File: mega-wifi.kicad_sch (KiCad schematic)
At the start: 25 parts, among them P2 MD-CART-FINGERS, U4 AZ1117CH-3.3, U5 74LVC1G08GW, U6 74LVC162245, U7 74LVC245, U8 74LVC162245

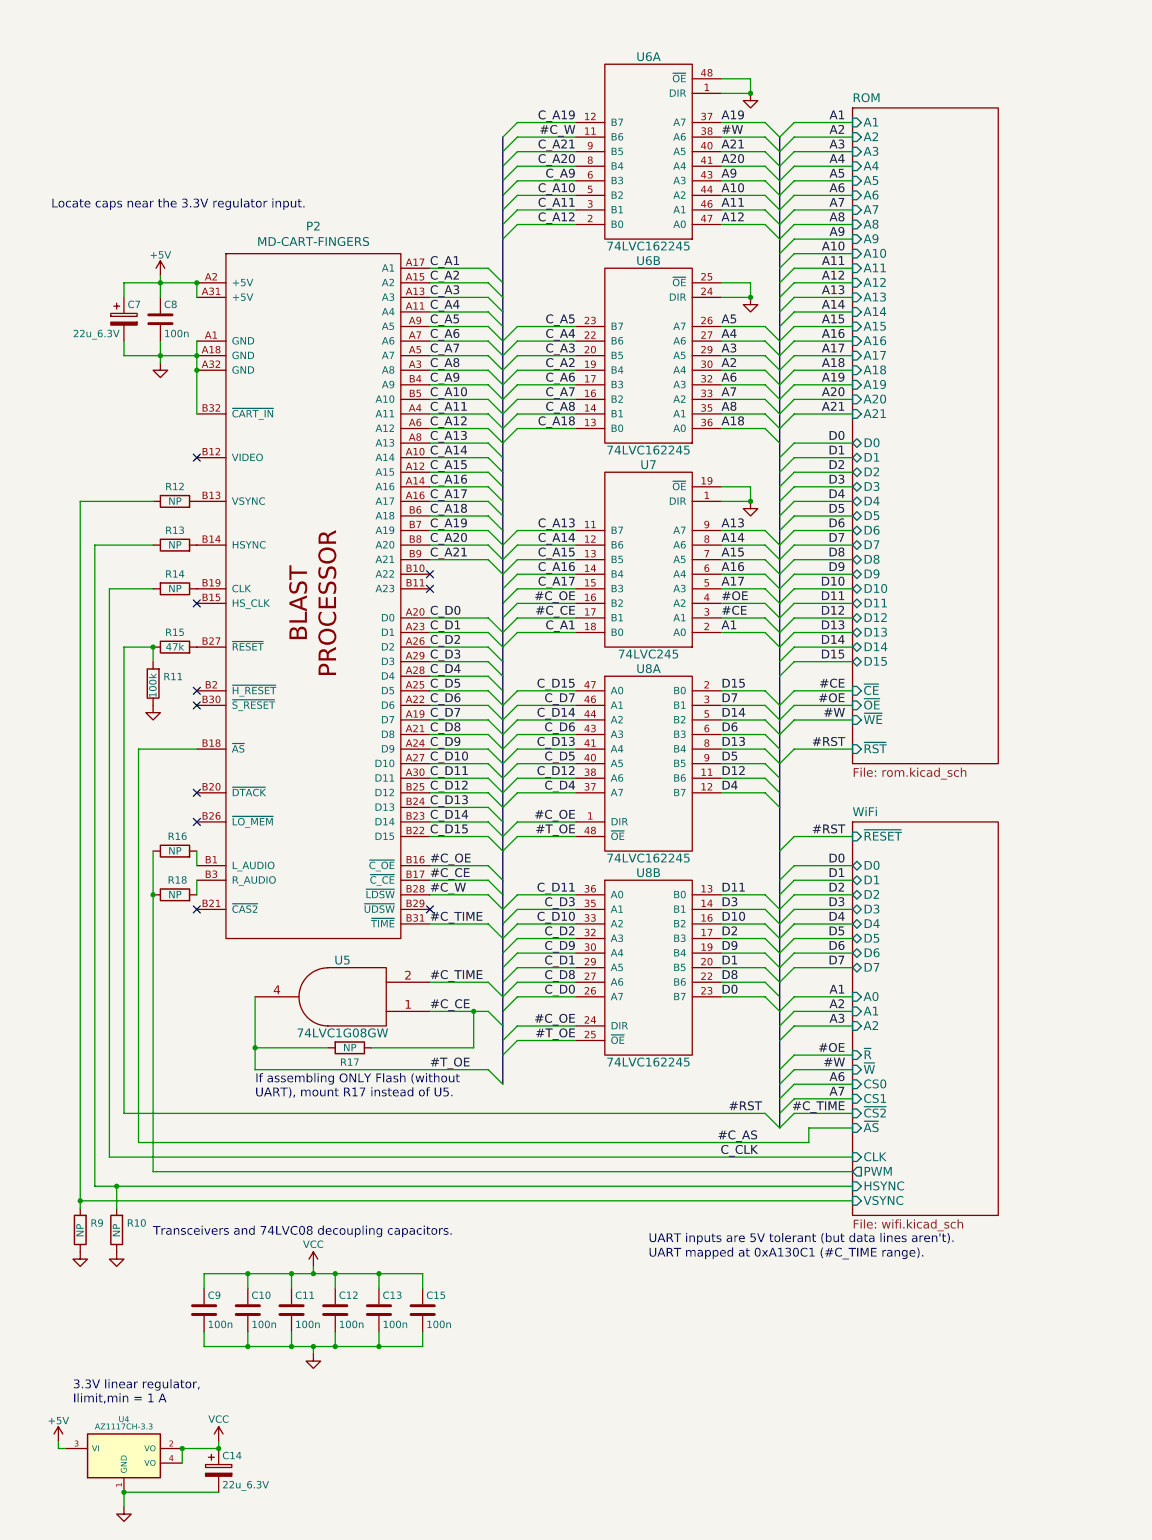
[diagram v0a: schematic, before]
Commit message: Update schematics for Rev.B:
* Switch obsolete SC16C554BIB48 with SC16C554BIBS
* Change ESP8266 with ESP32-C3
* Add USB-C connector for flashing/debugging
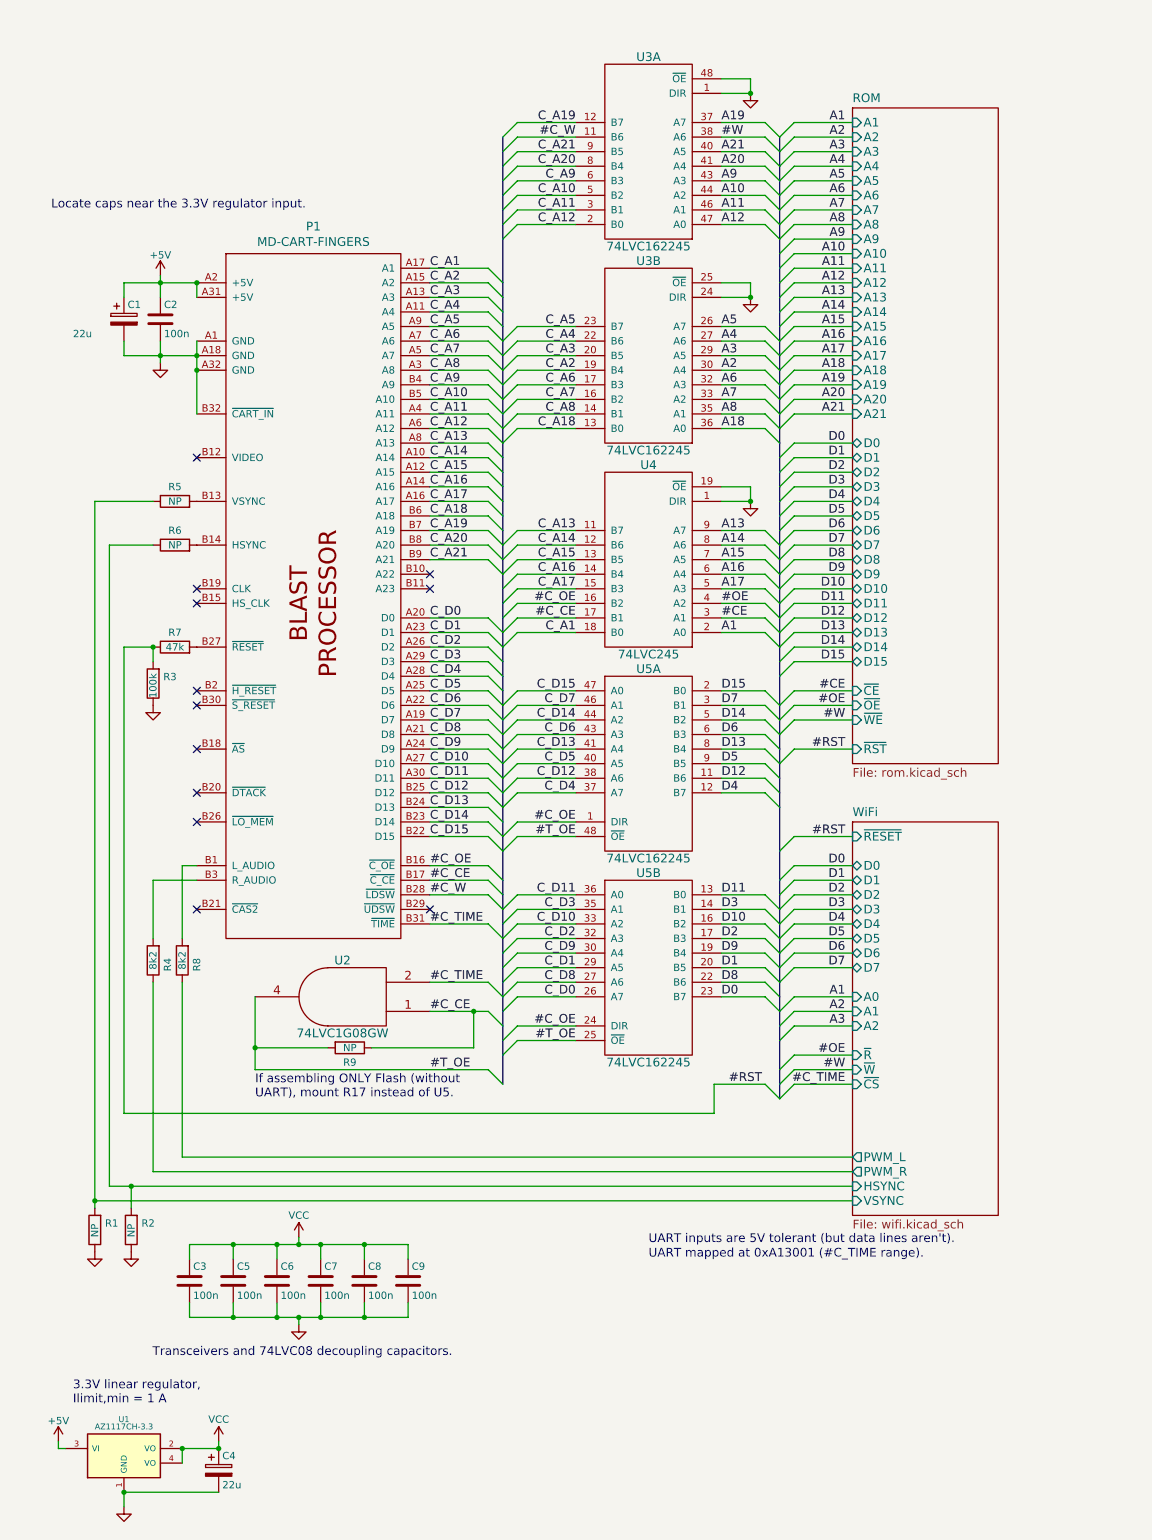
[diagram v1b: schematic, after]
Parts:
- removed R14, R16, R18: NP, doragasu:JUMPER_0805, symbol Device:R
- added R4, R8: 8k2, Resistor_SMD:R_0603_1608Metric, symbol Device:R
- C1: renamed from C7; value 22u_6.3V -> 22u; footprint Capacitors_SMD:c_elec_4x4.5 -> Capacitor_SMD:C_1206_3216Metric; LCSC# C250865 -> C12891
- C2: renamed from C8; footprint Capacitors_SMD:C_0805 -> Capacitor_SMD:C_0603_1608Metric; LCSC# C2830722 -> C14663
- C3: renamed from C9; footprint Capacitors_SMD:C_0805 -> Capacitor_SMD:C_0603_1608Metric; LCSC# C2830722 -> C14663
- C4: renamed from C14; value 22u_6.3V -> 22u; footprint Capacitors_SMD:c_elec_4x4.5 -> Capacitor_SMD:C_1206_3216Metric; LCSC# C250865 -> C12891
- C5: renamed from C10; footprint Capacitors_SMD:C_0805 -> Capacitor_SMD:C_0603_1608Metric; LCSC# C2830722 -> C14663
- C6: renamed from C11; footprint Capacitors_SMD:C_0805 -> Capacitor_SMD:C_0603_1608Metric; LCSC# C2830722 -> C14663
- C7: renamed from C12; footprint Capacitors_SMD:C_0805 -> Capacitor_SMD:C_0603_1608Metric; LCSC# C2830722 -> C14663
- C8: renamed from C13; footprint Capacitors_SMD:C_0805 -> Capacitor_SMD:C_0603_1608Metric; LCSC# C2830722 -> C14663
- C9: renamed from C15; footprint Capacitors_SMD:C_0805 -> Capacitor_SMD:C_0603_1608Metric; LCSC# C2830722 -> C14663
- R1: renamed from R9; footprint Resistors_SMD:R_0805 -> Resistor_SMD:R_0603_1608Metric
- R2: renamed from R10; footprint Resistors_SMD:R_0805 -> Resistor_SMD:R_0603_1608Metric
- R3: renamed from R11; footprint Resistors_SMD:R_0805 -> Resistor_SMD:R_0603_1608Metric; LCSC# C237121 -> C25803
- R5: renamed from R12; footprint Resistors_SMD:R_0805 -> Resistor_SMD:R_0603_1608Metric
- R6: renamed from R13; footprint Resistors_SMD:R_0805 -> Resistor_SMD:R_0603_1608Metric
- R7: renamed from R15; footprint Resistors_SMD:R_0805 -> Resistor_SMD:R_0603_1608Metric; LCSC# C144558 -> C25819
- U1: renamed from U4; footprint SMD_Packages:SOT-223 -> Package_TO_SOT_SMD:SOT-223; LCSC# C351784 -> C6186
- U2: renamed from U5; footprint Housings_SOT-23_SOT-143_TSOT-6:SOT23-5 -> Package_TO_SOT_SMD:SOT-23-5
- U3: renamed from U6; footprint Housings_SSOP:TSSOP-48_6.1x12.5mm_Pitch0.5mm -> Package_SO:TSSOP-48_6.1x12.5mm_P0.5mm
- U4: renamed from U7; footprint Housings_SSOP:SSOP-20_4.4x6.5mm_Pitch0.65mm -> Package_SO:SSOP-20_4.4x6.5mm_P0.65mm
- U5: renamed from U8; footprint Housings_SSOP:TSSOP-48_6.1x12.5mm_Pitch0.5mm -> Package_SO:TSSOP-48_6.1x12.5mm_P0.5mm
- renumbered P2 to P1, R17 to R9
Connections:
- net at P1.B1 (L_AUDIO): now also R8.2
- net at P1.B3 (R_AUDIO): now also R4.2
- net #C_AS: no longer names the net of P1.B18 (~{AS})
- new net WiFi/PWM_L: R8.1
- new net WiFi/PWM_R: R4.1
- no-connect marks 10 -> 12
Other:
- sheet WiFi ports: added PWM_L, PWM_R, ~{CS}; removed CLK, CS0, CS1, PWM, ~{AS}, ~{CS2}
- note added: "UART mapped at 0xA13001 (#C_TIME range)."
- note removed: "UART mapped at 0xA130C1 (#C_TIME range)."
- moved on the sheet: C3, C5, C6, C7, C8, C9, R1, R2

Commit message: Rev.B PCB
* Replace obsolete SC16C550BIB48 with SC16C550BIBS
* Replace ESP8266 with ESP32-C3
* Implement 64 Mbit hack
* Add USB-C debug header for ESP32-C3
* Many PCB improvements
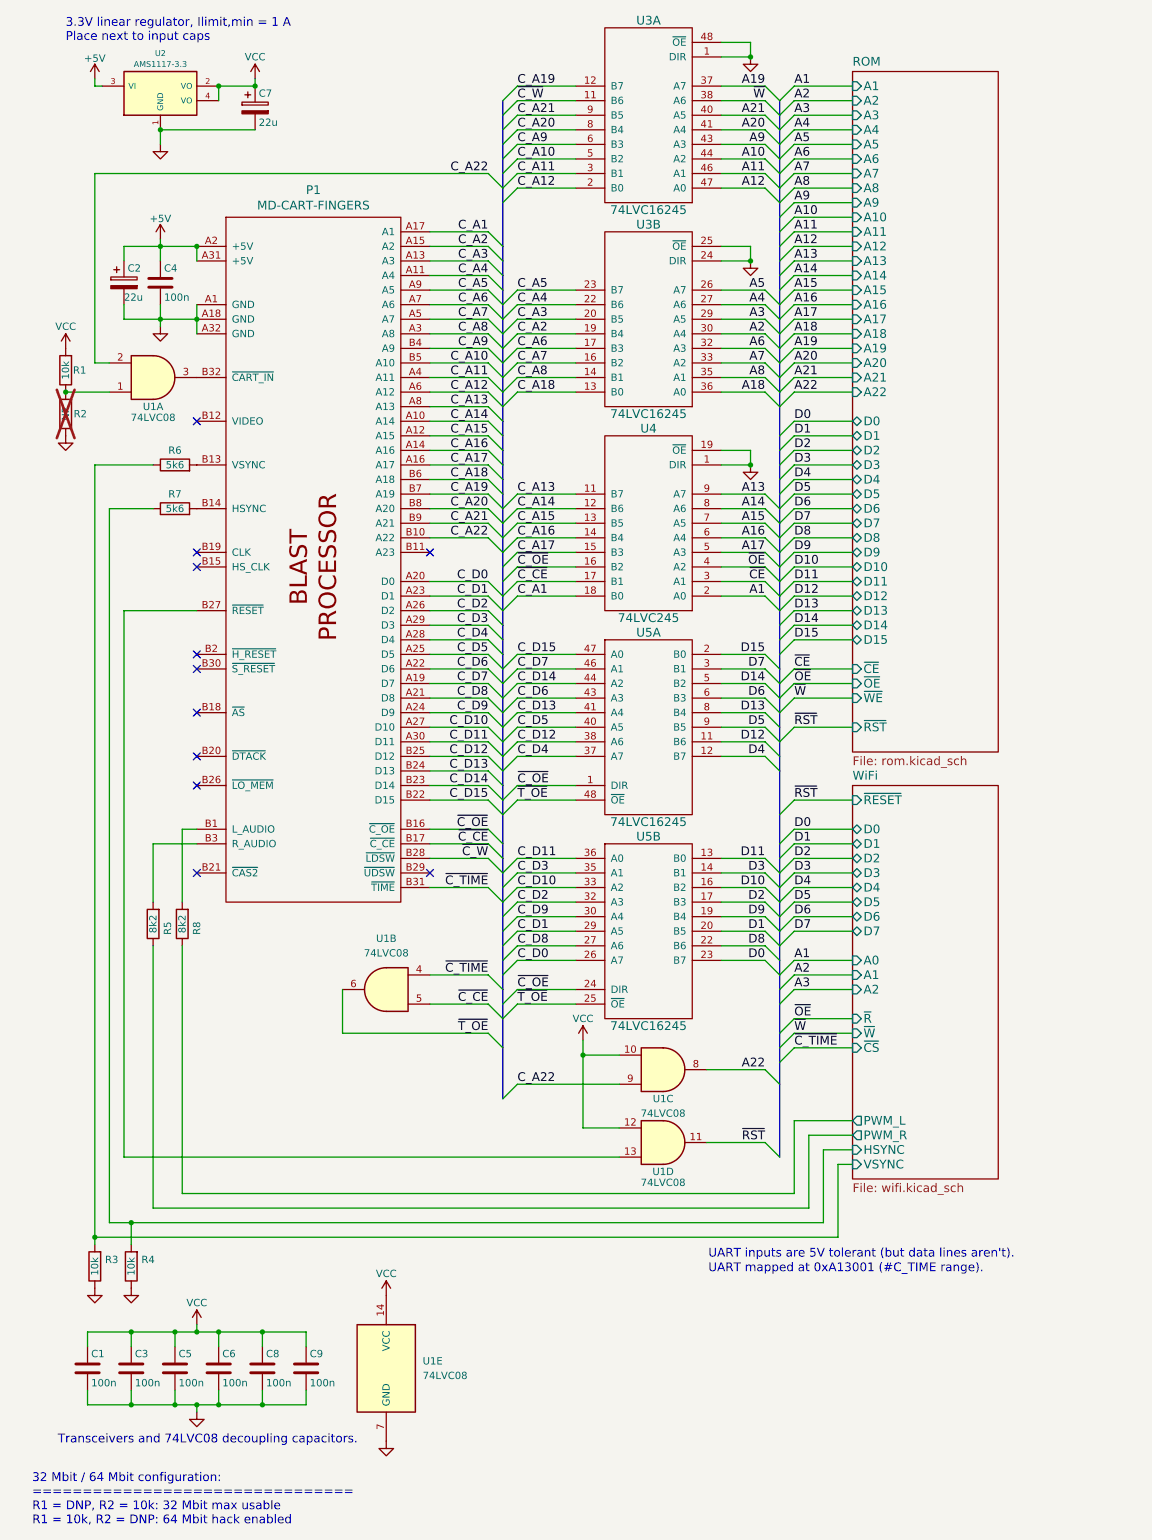
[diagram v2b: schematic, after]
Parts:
- removed R3: 100k, Resistor_SMD:R_0603_1608Metric, symbol Device:R
- removed R7: 47k, Resistor_SMD:R_0603_1608Metric, symbol Device:R
- removed R9: NP, doragasu:JUMPER_0805, symbol Device:R
- removed U2: 74LVC1G08GW, Package_TO_SOT_SMD:SOT-23-5, symbol doragasu:74LVC1G08GW
- added R1: 10k, Resistor_SMD:R_0603_1608Metric, symbol Device:R
- added R2: NP, Resistor_SMD:R_0603_1608Metric, symbol Device:R
- added U1: 74LVC08, Package_SO:TSSOP-14_4.4x5mm_P0.65mm, symbol 74xx:74LS08
- R3: renamed from R1; value NP -> 10k; LCSC# (none) -> C25804
- R4: renamed from R2; value NP -> 10k; LCSC# (none) -> C25804
- R6: renamed from R5; value NP -> 5k6; LCSC# (none) -> C23189
- R7: renamed from R6; value NP -> 5k6; LCSC# (none) -> C23189
- U2: renamed from U1; value AZ1117CH-3.3 -> AMS1117-3.3
- U3, U5: value 74LVC162245 -> 74LVC16245; LCSC# C6069 -> C7824
- U4: footprint Package_SO:SSOP-20_4.4x6.5mm_P0.65mm -> Package_SO:TSSOP-20_4.4x6.5mm_P0.65mm; LCSC# C393617 -> C7848
- renumbered C3 to C1, C1 to C2, C5 to C3, C2 to C4, C6 to C5, C7 to C6, C4 to C7, R4 to R5
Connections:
- net GND: now also R2.1, U1.7 (GND); no longer P1.B32 (~{CART_IN})
- net VCC: now also R1.2, U1.10, U1.12, U1.14 (VCC)
- net C_A22: now reaches P1.B10 (A22)
- net C_A22: now also U1.2, U1.9
- net at P1.B27 (~{RESET}): now also U1.13
- net #CE renamed ~{CE}
- net #C_CE renamed ~{C_CE}
- net ~{C_CE}: now also U1.5
- net #C_OE renamed ~{C_OE}
- net #C_TIME renamed ~{C_TIME}
- net ~{C_TIME}: now also U1.4
- net #C_W renamed ~{C_W}
- net #OE renamed ~{OE}
- net #T_OE renamed ~{T_OE}
- net ~{T_OE}: now also U1.6
- net #W renamed ~{W}
- new net: P1.B32 (~{CART_IN}), U1.3
- new net: R1.1, R2.2, U1.1
- new net A22: U1.8
- new net ~{RST}: U1.11
- no-connect marks 12 -> 11
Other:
- sheet ROM ports: added A22; removed none
- note added: "3.3V linear regulator, Ilimit,min = 1 A Place next to input caps"
- note added: "32 Mbit / 64 Mbit configuration: ================================ R1 = DNP, R2 = 10k: 32 Mbit max usable R1 = 10k, R2 = DNP: 64 Mbit hack enabled"
- note removed: "3.3V linear regulator, Ilimit,min = 1 A"
- note removed: "If assembling ONLY Flash (without UART), mount R17 instead of U5."
- note removed: "Locate caps near the 3.3V regulator input."
- moved on the sheet: C1, C2, C3, C4, C5, C6, C7, C8, C9, P1, R3, R4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

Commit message: Fabrication tweaks
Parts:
- R1: value 10k -> 0R0; LCSC# C25804 -> C21189
- R3, R4, R6, R7: Config DNF -> (none)
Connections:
- net C_A22: now also R1.2; no longer U1.2
- net GND: now also U1.1, U1.2
- net VCC: no longer R1.2
- net at P1.B32 (~{CART_IN}): now also R1.1, R2.2; no longer U1.3
- no-connect marks 11 -> 12
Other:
- note added: "32 Mbit / 64 Mbit configuration: ================================ R1 = DNP, R2 = 0R0: 32 Mbit max usable R1 = 0R0, R2 = DNP: 64 Mbit hack enabled (default)"
- note removed: "32 Mbit / 64 Mbit configuration: ================================ R1 = DNP, R2 = 10k: 32 Mbit max usable R1 = 10k, R2 = DNP: 64 Mbit hack enabled"
- moved on the sheet: R1, R2, U1A

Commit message: Allow ESP32 to reset the host
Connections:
- net ~{C_RST}: now reaches P1.B27 (~{RESET}), U1.13
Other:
- moved on the sheet: R3, R4
